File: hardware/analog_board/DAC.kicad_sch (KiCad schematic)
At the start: 120 parts, among them Q1 MMBT3906, Q2 MMBT3906, U3 AD9747BCPZ, U4 OPA695ID, U5 OPA695ID, U6 NE5532

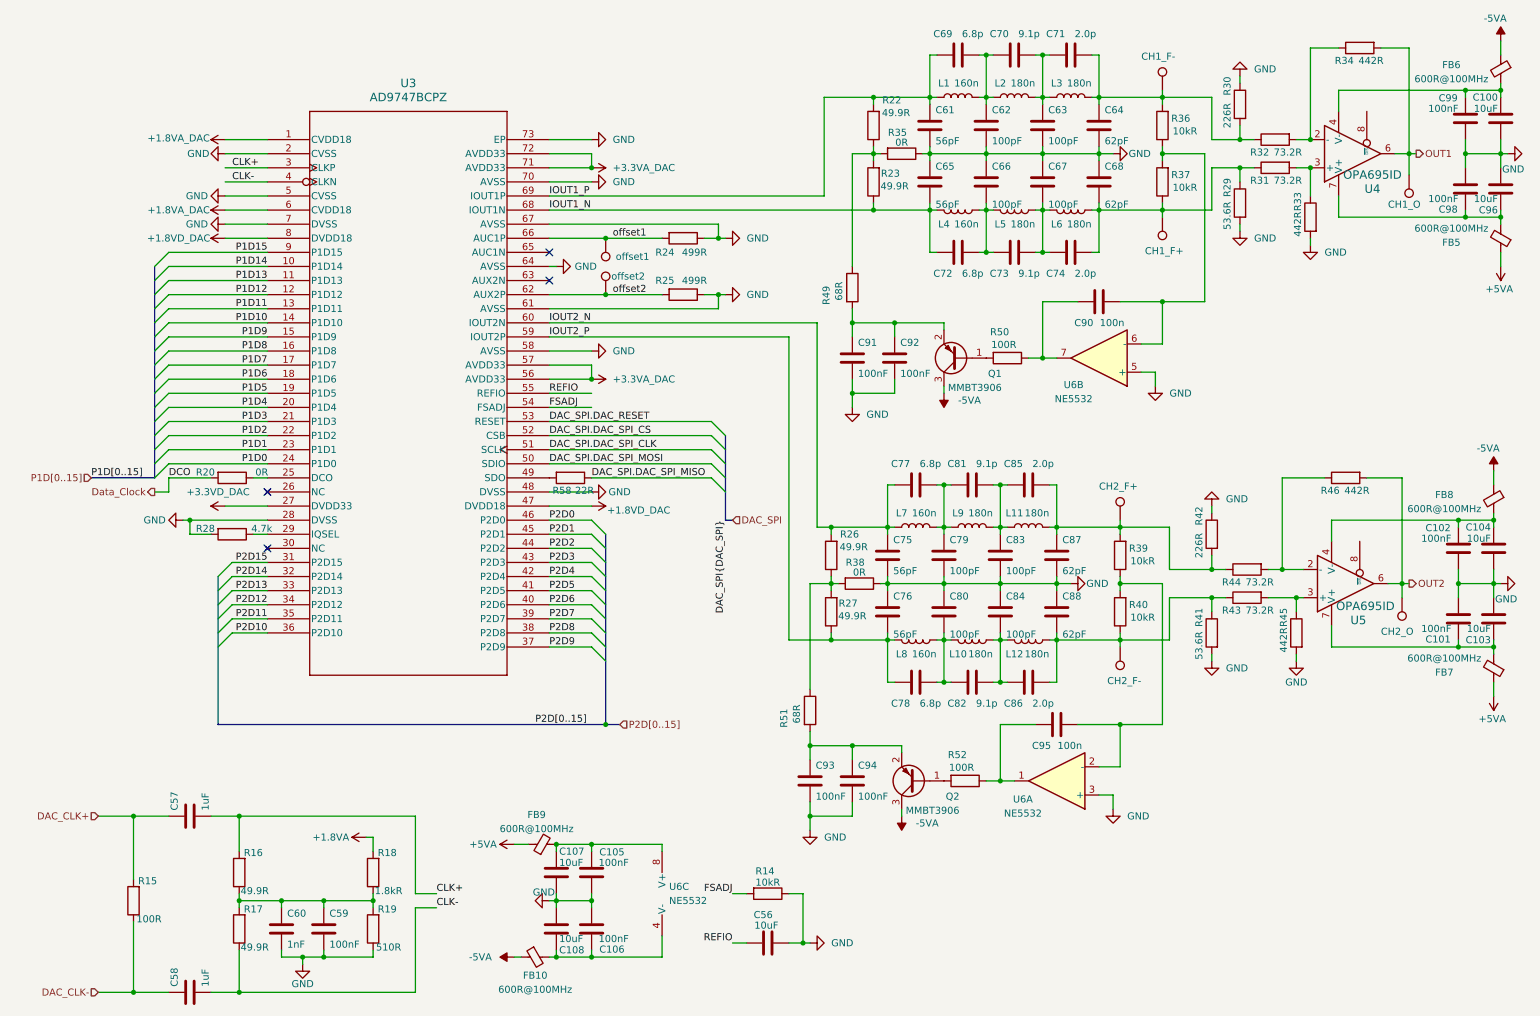
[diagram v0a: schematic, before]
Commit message: debug：修正原理图部分错误
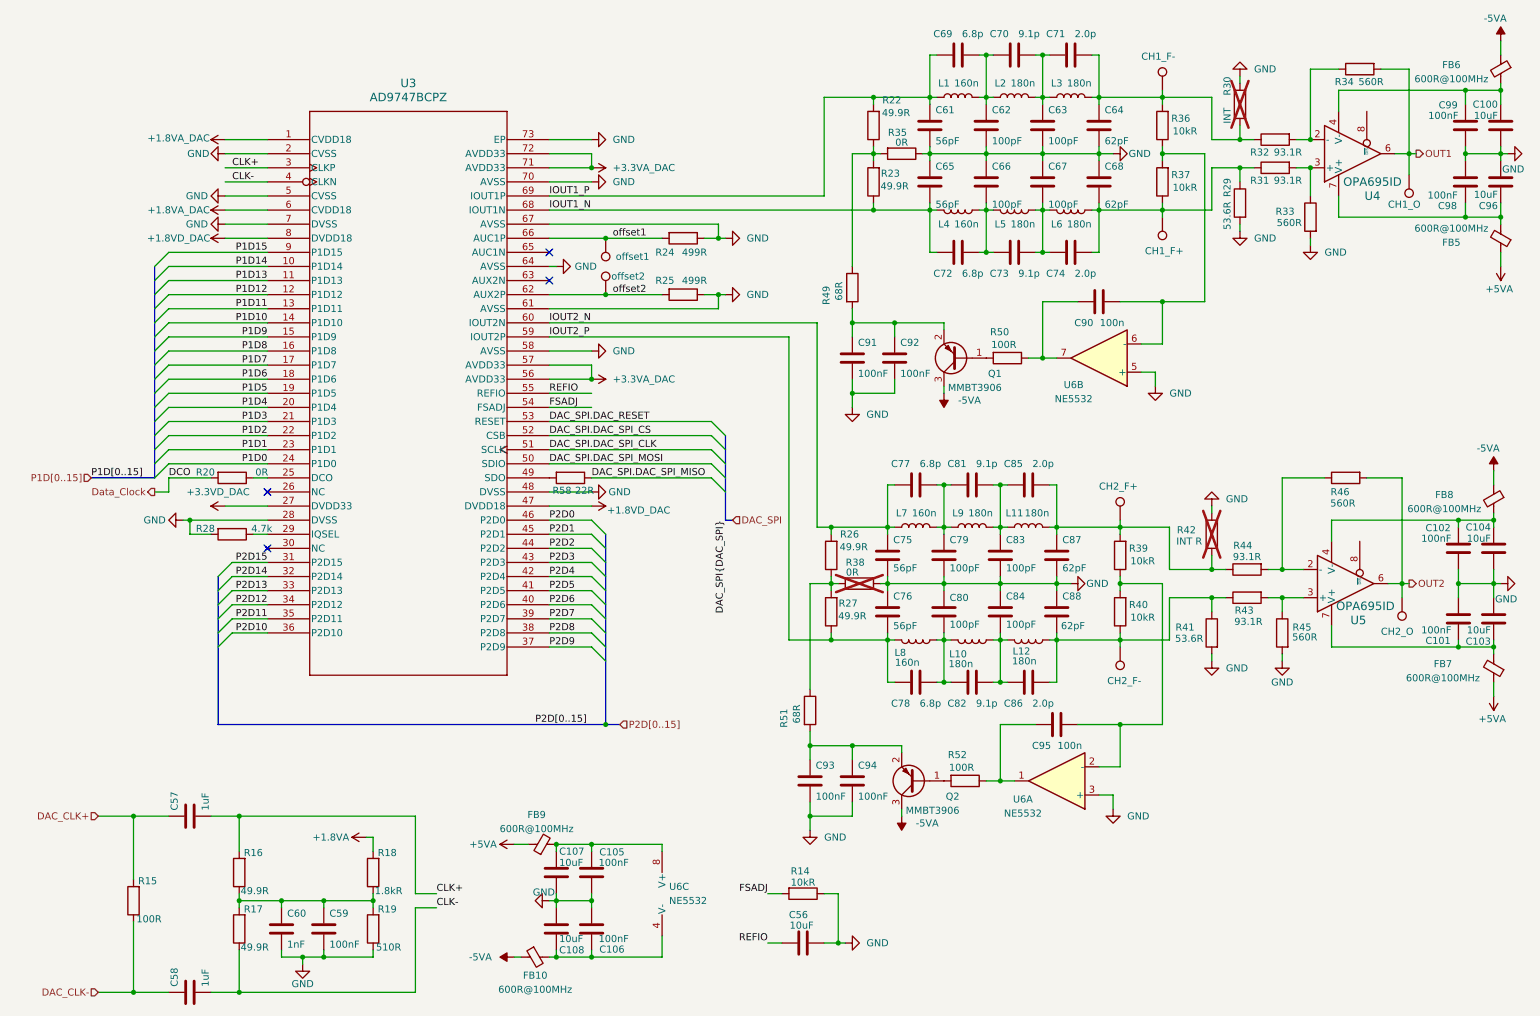
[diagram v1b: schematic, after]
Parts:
- R30: value 226R -> INT; now not fitted
- R31, R32, R43, R44: value 73.2R -> 93.1R
- R33, R34, R45, R46: value 442R -> 560R
- R38: now not fitted; now left out of the parts list
- R42: value 226R -> INT R; now not fitted; now left out of the parts list
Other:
- moved on the sheet: C100, C56, C96, C98, C99, R14, R34, R45

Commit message: feat：BOM导出
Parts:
- R30: now left out of the parts list
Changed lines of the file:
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@@
 		(body_style 1)
 		(exclude_from_sim no)
-		(in_bom yes)
+		(in_bom no)
 		(on_board yes)
 		(in_pos_files yes)
